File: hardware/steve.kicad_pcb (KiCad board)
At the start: 4 copper layers, 70 x 120 mm, 86 parts, among them J1 Conn_ARM_SWD_TagConnect_TC203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, J2 Conn_01x06, J3 Conn_01x06, J4 TerminalBlock_1770979_4pos_Ve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, J5 USB_C_Receptacle_16P, J6 MicroSD_Hirose_DM3AT, J7 TerminalBlock_1770885_2pos, J8 Conn_01x06, Q1 Q_NMOS_GSD, Q2 Q_NMOS_GSD, Q3 Q_NMOS_GSD, Q4 Q_NMOS_GSD, Q5 Q_NMOS_GSD, Q6 Q_NMOS_GSD, SW1 KMR221G, SW2 KMR221G, U1 STM32F407VGTx, U3 TLV1117LV33DCYR, U4 BMI270, U5 BMP388/390, U6 W25Q128JVSIQ, Y1 8MHz, Y2 32.768kHz

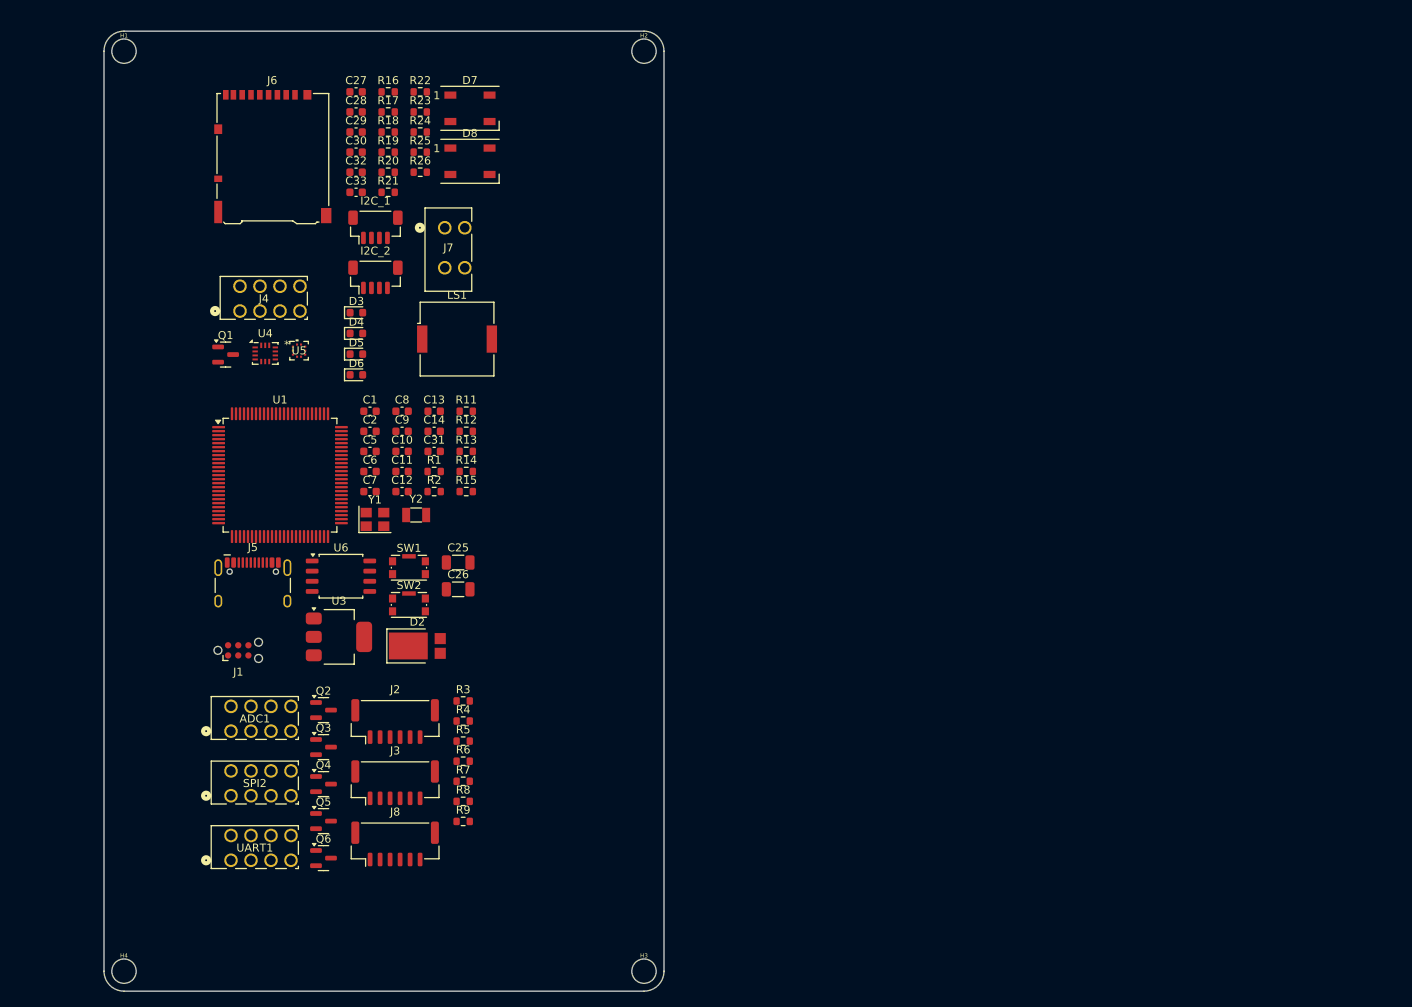
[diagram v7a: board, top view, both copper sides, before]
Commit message: started component layout
started component layout - attempting to use a 60x60mm board size
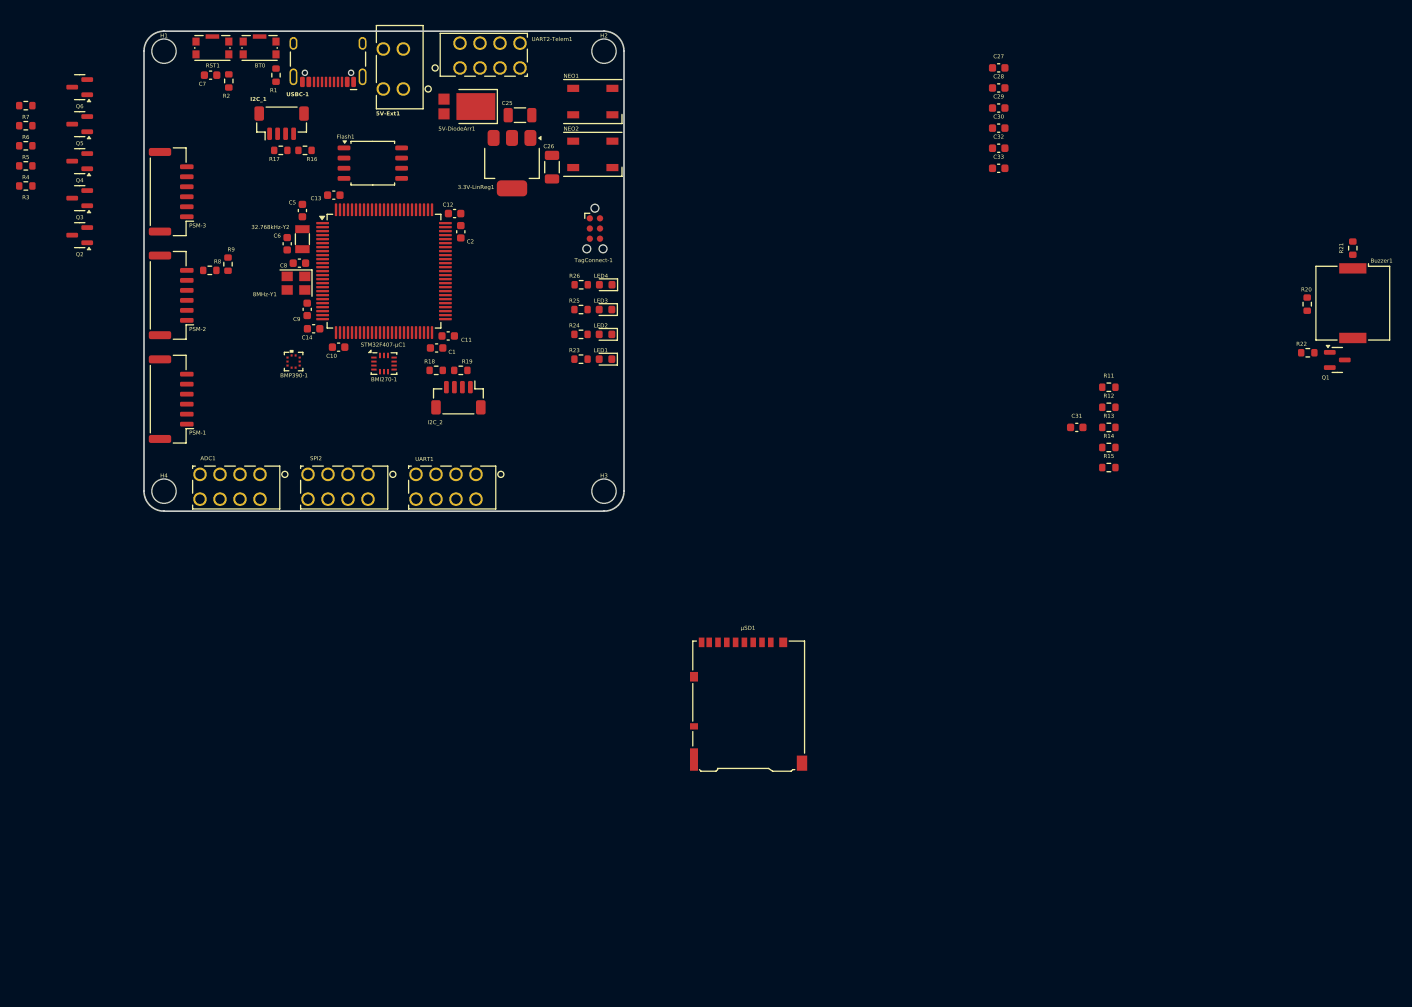
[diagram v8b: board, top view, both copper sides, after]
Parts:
- removed D3: RED, LED_SMD:LED_0603_1608Metric
- removed D4: Yellow, LED_SMD:LED_0603_1608Metric
- removed D5: GREEN, LED_SMD:LED_0603_1608Metric
- removed D6: BLUE, LED_SMD:LED_0603_1608Metric
- added LED1: RED, LED_SMD:LED_0603_1608Metric, F.Cu at (112.7, 91.0)
- added LED2: YELLOW, LED_SMD:LED_0603_1608Metric, F.Cu at (112.7, 87.9)
- added LED3: GREEN, LED_SMD:LED_0603_1608Metric, F.Cu at (112.7, 84.8)
- added LED4: BLUE, LED_SMD:LED_0603_1608Metric, F.Cu at (112.7, 81.7)
- BMP390-1: renamed from U5; value BMP388/390 -> BMP390
- PSM-1: renamed from J2; value Conn_01x06 -> PSM-Servo
- PSM-2: renamed from J3; value Conn_01x06 -> PSM-MOSFET_BATT1
- PSM-3: renamed from J8; value Conn_01x06 -> PSM_Cont
- TagConnect-1: renamed from J1; value Conn_ARM_SWD_TagConnect_TC2030-NL -> TagConnect_TC2030-NL
- moved Q1 139.0 mm to (204.2, 91.1)
- moved R21 120.8 mm to (206.1, 77.1), turned to 90 degrees
- moved R20 116.1 mm to (200.4, 84.1), turned to 90 degrees
- moved R22 115.6 mm to (200.5, 90.2)
- moved Buzzer1 112.1 mm to (206.1, 84.0), turned to -90 degrees
- moved Q6 101.1 mm to (47.0, 57.0), turned to 180 degrees
- moved R7 100.6 mm to (40.2, 59.3), turned to 180 degrees
- moved R6 96.4 mm to (40.2, 61.8), turned to 180 degrees
- moved R5 92.3 mm to (40.2, 64.3), turned to 180 degrees
- moved Q5 92.3 mm to (47.0, 61.6), turned to 180 degrees
- moved µSD1 90.7 mm to (130.6, 134.1)
- moved R4 88.3 mm to (40.2, 66.8), turned to 180 degrees
- moved PSM-3 86.2 mm to (58.4, 70.1), turned to 90 degrees
- moved R3 84.5 mm to (40.2, 69.3), turned to 180 degrees
- moved Q4 83.6 mm to (47.0, 66.2), turned to 180 degrees
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- renumbered U3 to 3.3V-LinReg1, Y2 to 32.768kHz-Y2, D2 to 5V-DiodeArr1, J7 to 5V-Ext1, Y1 to 8MHz-Y1, U4 to BMI270-1, SW2 to BT0, LS1 to Buzzer1, U6 to Flash1, D7 to NEO1, D8 to NEO2, SW1 to RST1, U1 to STM32F407-µC1, J4 to UART2-Telem1, J5 to USBC-1, J6 to µSD1
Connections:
- 3.3V-LinReg1 pad 1: HSE_OSC_IN -> GND
- 5V-Ext1 pad 3: HSE_OSC_IN -> GND
- 5V-Ext1 pad 4: HSE_OSC_IN -> GND
- 8MHz-Y1 pad 2: HSE_OSC_IN -> GND
- 8MHz-Y1 pad 3: HSE_OSC_IN -> HSE_OSC_OUT
- 8MHz-Y1 pad 4: HSE_OSC_IN -> GND
- ADC1 pad 1: HSE_OSC_IN -> GND
- ADC1 pad 2: HSE_OSC_IN -> GND
- BMI270-1 pad 6: HSE_OSC_IN -> GND
- BMI270-1 pad 7: HSE_OSC_IN -> GND
- BMP390-1 pad 3: HSE_OSC_IN -> GND
- BMP390-1 pad 8: HSE_OSC_IN -> GND
- BMP390-1 pad 9: HSE_OSC_IN -> GND
- BT0 pad SH: HSE_OSC_IN -> GND
- C1 pad 2: HSE_OSC_IN -> GND
- C10 pad 2: HSE_OSC_IN -> GND
- C11 pad 2: HSE_OSC_IN -> GND
- C12 pad 2: HSE_OSC_IN -> GND
- C13 pad 2: HSE_OSC_IN -> GND
- C14 pad 2: HSE_OSC_IN -> GND
- C2 pad 2: HSE_OSC_IN -> GND
- C25 pad 2: HSE_OSC_IN -> GND
- C26 pad 2: HSE_OSC_IN -> GND
- C27 pad 2: HSE_OSC_IN -> GND
- C28 pad 2: HSE_OSC_IN -> GND
- C29 pad 2: HSE_OSC_IN -> GND
- C30 pad 2: HSE_OSC_IN -> GND
- C31 pad 2: HSE_OSC_IN -> GND
- C32 pad 2: HSE_OSC_IN -> GND
- C33 pad 2: HSE_OSC_IN -> GND
- C5 pad 2: HSE_OSC_IN -> GND
- C6 pad 2: HSE_OSC_IN -> GND
- C7 pad 2: HSE_OSC_IN -> GND
- C8 pad 2: HSE_OSC_IN -> GND
- C9 pad 2: HSE_OSC_IN -> GND
- Flash1 pad 4: HSE_OSC_IN -> GND
- I2C_1 pad 1: HSE_OSC_IN -> GND
- I2C_2 pad 1: HSE_OSC_IN -> GND
- NEO1 pad 3: HSE_OSC_IN -> GND
- NEO2 pad 3: HSE_OSC_IN -> GND
- Q1 pad 2: HSE_OSC_IN -> GND
- Q2 pad 2: HSE_OSC_IN -> GND
- Q3 pad 2: HSE_OSC_IN -> GND
- Q4 pad 2: HSE_OSC_IN -> GND
- Q5 pad 2: HSE_OSC_IN -> GND
- Q6 pad 2: HSE_OSC_IN -> GND
- R1 pad 2: HSE_OSC_IN -> GND
- R13 pad 2: HSE_OSC_IN -> GND
- R14 pad 2: HSE_OSC_IN -> GND
- R9 pad 1: HSE_OSC_IN -> GND
- RST1 pad 2: HSE_OSC_IN -> GND
- RST1 pad SH: HSE_OSC_IN -> GND
- SPI2 pad 1: HSE_OSC_IN -> GND
- SPI2 pad 2: HSE_OSC_IN -> GND
- STM32F407-µC1 pad 10: HSE_OSC_IN -> GND
- STM32F407-µC1 pad 13: HSE_OSC_IN -> HSE_OSC_OUT
- STM32F407-µC1 pad 20: HSE_OSC_IN -> GND
- STM32F407-µC1 pad 27: HSE_OSC_IN -> GND
- STM32F407-µC1 pad 74: HSE_OSC_IN -> GND
- STM32F407-µC1 pad 99: HSE_OSC_IN -> GND
- TagConnect-1 pad 5: HSE_OSC_IN -> GND
- UART1 pad 1: HSE_OSC_IN -> GND
- UART1 pad 2: HSE_OSC_IN -> GND
- UART2-Telem1 pad 1: HSE_OSC_IN -> GND
- UART2-Telem1 pad 2: HSE_OSC_IN -> GND
- USBC-1 pad A1: HSE_OSC_IN -> GND
- USBC-1 pad A12: HSE_OSC_IN -> GND
- USBC-1 pad B1: HSE_OSC_IN -> GND
- USBC-1 pad B12: HSE_OSC_IN -> GND
- USBC-1 pad S1: HSE_OSC_IN -> GND
- µSD1 pad 11: HSE_OSC_IN -> GND
- µSD1 pad 6: HSE_OSC_IN -> GND
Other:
- board size 70 x 120 mm -> 60 x 60 mm
